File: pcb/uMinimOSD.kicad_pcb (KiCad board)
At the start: 2 copper layers, 36 x 36 mm, 48 parts, among them P1 CONN_01X05, P2 CONN_01X04, P3 CONN_01X06, P4 CONN_01X06, P5 CONN_01X02, P6 CONN_01X06, Q1 Q_NMOS_GSD, U1 TPS2112

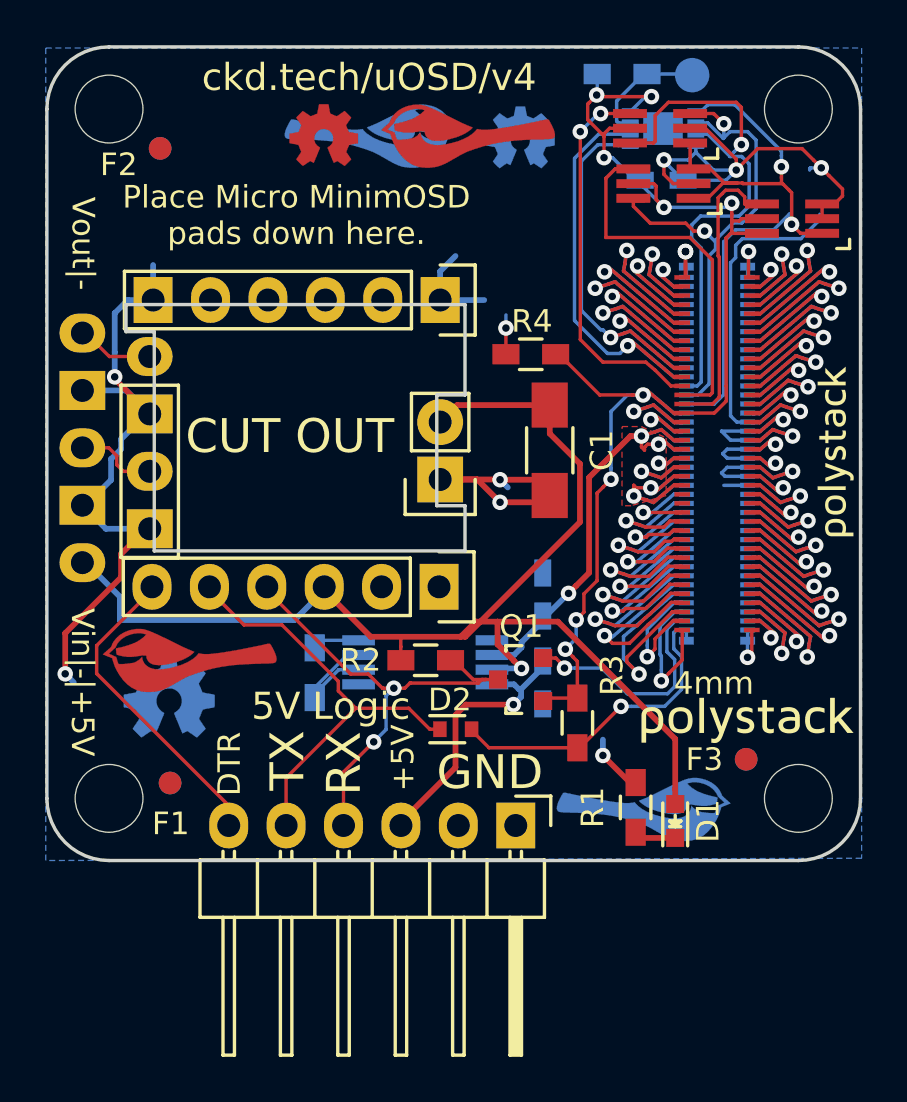
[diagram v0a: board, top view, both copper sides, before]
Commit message: Remove extra chickadee logo, pdate polystack logo to bold variant, connect i2c lines to eeprom and bump version number.
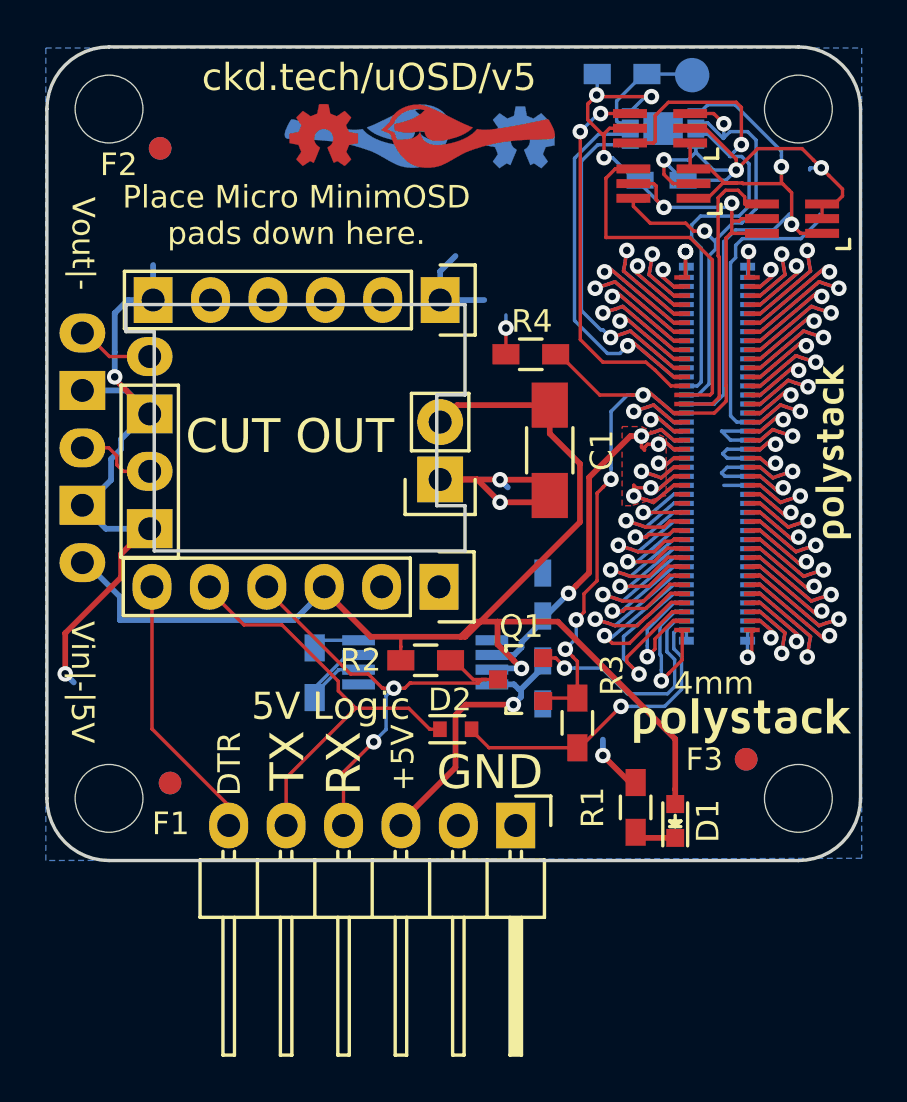
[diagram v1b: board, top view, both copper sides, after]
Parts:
- removed the G*** at (136.3, 117.1)
- removed the G*** at (156.4, 123.7)
- removed the G*** at (135.4, 118.7)
- svg2mod (x2): footprint polystack:polystack-medium-0.5 -> polystack:polystack-bold-0.5
- svg2mod (x2): footprint polystack:polystack-medium-0.4 -> polystack:polystack-bold-0.4
- moved svg2mod 0.22 mm to (160.8, 119.8)
- moved svg2mod 0.17 mm to (160.8, 119.8)
- moved svg2mod 0.10 mm to (164.8, 107.9) (x2)
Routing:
- net /DTR: track 14.0 -> 12.0 mm
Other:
- board text added: "5V|-|Vin"
- board text added: "Vin|-|5V"
- board text added: "ckd.tech/uOSD/v5"
- board text removed: "+5V|-|Vin"
- board text removed: "Vin|-|+5V"
- board text removed: "ckd.tech/uOSD/v4"

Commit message: Add license information to many files. PCB design files are CC-BY and code is MIT license.
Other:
- board text added: "Copyright 2016 Chickadee Tech LLC, <add attributions here> This work is licensed under the Creative Commons Attribution 4.0 International License. To view a copy of this license, visit http://creativecommons.org/licenses/by/4.0/ or send a letter to Creative Commons, PO Box 1866, Mountain View, CA 94042, USA."
- board text added: "Remove all Chickadee Tech LLC trademarks before making your own board. The Chickadee logo and Polystack logo are owned by Chickadee Tech LLC. You may license the Polystack logo for free by emailing support@chickadee.tech and receiving express written permission from Chickadee Tech LLC."
- board text added: "The gear logo is a mark designating open source hardware. Remove it if your design does not comply with the open source hardware definition."
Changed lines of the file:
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@@
     (links 167)
     (no_connects 0)
-    (area 129.924999 89.924999 166.075001 126.075001)
+    (area 67.49 74.1 280.940001 192.01)
     (thickness 1.6)
-    (drawings 58)
+    (drawings 66)
     (tracks 1087)
     (zones 0)
@@
     (40 Dwgs.User user)
     (41 Cmts.User user)
-    (42 Eco1.User user hide)
-    (43 Eco2.User user hide)
+    (42 Eco1.User user)
+    (43 Eco2.User user)
     (44 Edge.Cuts user)
     (45 Margin user)
@@
       (xy 2.990233 -0.444493)) (layer B.SilkS) (width 0))
   )
+  (gr_line (start 166.69 114.65) (end 142.89 94.99) (layer Cmts.User) (width 0.2))
+  (gr_line (start 151.74 95.56) (end 166.69 114.65) (layer Cmts.User) (width 0.2))
+  (gr_text "The gear logo is a mark designating open\nsource hardware. Remove it if your design\ndoes not comply with the open source\nhardware definition." (at 167.72 115.57) (layer Cmts.User)
+    (effects (font (size 1.5 1.5) (thickness 0.3)) (justify left))
+  )
+  (gr_line (start 108.8 108.72) (end 162.95 108.1) (layer Cmts.User) (width 0.2))
+  (gr_line (start 108.63 108.62) (end 155.7 119.62) (layer Cmts.User) (width 0.2))
+  (gr_line (start 144.64 95.23) (end 108.63 108.62) (layer Cmts.User) (width 0.2))
+  (gr_text "Remove all Chickadee Tech LLC trademarks\nbefore making your own board. The\nChickadee logo and Polystack logo\nare owned by Chickadee Tech LLC.\n\nYou may license the Polystack logo for\nfree by emailing support@chickadee.tech\nand receiving express written permission\nfrom Chickadee Tech LLC." (at 67.64 109.97) (layer Cmts.User)
+    (effects (font (size 1.5 1.5) (thickness 0.3)) (justify left))
+  )
+  (gr_text "Copyright 2016 Chickadee Tech LLC, <add attributions here>\n\nThis work is licensed under the Creative Commons Attribution 4.0 International License.\nTo view a copy of this license, visit http://creativecommons.org/licenses/by/4.0/\nor send a letter to Creative Commons, PO Box 1866, Mountain View, CA 94042, USA." (at 179.29 173.95) (layer Cmts.User)
+    (effects (font (size 1.5 1.5) (thickness 0.3)) (justify left))
+  )
   (gr_circle (center 143.55 119.29) (end 143.84 119.54) (layer B.SilkS) (width 0.2))
   (gr_text "5V Logic" (at 142.56 119.175) (layer F.SilkS)
@@
   (gr_line (start 134.75 102.6) (end 134.75 112.3) (layer Edge.Cuts) (width 0.15))
   (gr_line (start 133.5 101.4) (end 148.5 101.4) (layer Edge.Cuts) (width 0.15))
-  (gr_text "Board is\n15.1mm x\n15.2mm." (at 110.01 105.18) (layer Cmts.User)
+  (gr_text "Board is\n15.1mm x\n15.2mm." (at 141.34 107.37) (layer Cmts.User)
     (effects (font (size 1.5 1.5) (thickness 0.3)))
   )
@@
     (effects (font (size 1.5 1.5) (thickness 0.3)))
   )
-  (gr_text Front (at 121.17 108.99) (layer Cmts.User)
+  (gr_text Front (at 126.31 105.82) (layer Cmts.User)
     (effects (font (size 1.5 1.5) (thickness 0.3)))
   )
@@
   (gr_line (start 166 92.75) (end 166 123.25) (angle 90) (layer Edge.Cuts) (width 0.15))
   (gr_line (start 132.75 90) (end 163.25 90) (angle 90) (layer Edge.Cuts) (width 0.15))
-  (gr_text uMinimOSD (at 187.25 174.25) (layer Cmts.User)
-    (effects (font (size 5 5) (thickness 0.5)) (justify left))
+  (gr_text uMinimOSD (at 187 189.66) (layer Cmts.User)
+    (effects (font (size 3 3) (thickness 0.5)) (justify left))
   )
   (segment (start 162.95 97.849974) (end 162.95 96.45) (width 0.1524) (layer F.Cu) (net 1))
